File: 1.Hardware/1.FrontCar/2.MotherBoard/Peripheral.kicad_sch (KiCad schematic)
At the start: 11 parts

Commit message: update .gitignore
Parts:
- removed C? (x2): 0.1uF, symbol Device:C_Small
- removed Q?: S8050, Package_TO_SOT_SMD:SOT-23, symbol Device:Q_NPN_BEC
- removed R?: 1K, symbol Device:R_Small
- removed R?: 10K, symbol Device:R_Small
- removed R?: 10R, symbol Device:R_Small
- removed SW?: SW_DIP_x04, symbol Switch:SW_DIP_x04
- removed U?: IPS114, ErBW_s:IPS114, symbol ErBW_s:IPS114
- added BZ?: (no value), symbol Device:Buzzer
- added C?: 100nF, Capacitor_SMD:C_0603_1608Metric, symbol Device:C_Small
- added Q?: (no value), symbol Transistor_BJT:S8050
- added R?: 5K1, symbol Device:R_Small
- IC?: value SN74LVC244APW -> (none); footprint SOP65P640X120-20N -> (none)
- SW?: value SW_5DIR -> (none); footprint ErBW_s:SW_5DIR -> (none)
- U?: value MT9V034 -> (none); footprint Connector_FFC-FPC:Hirose_FH12-18S-0.5SH_1x18-1MP_P0.50mm_Horizontal -> (none)
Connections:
- net GND: now also IC?.1 (1~{OE}), IC?.19 (2~{OE}), SW?.1 (GND), U?.16 (GND), U?.2 (GND), U?.7 (GND), U?.MP (NC), C?.2, Q?.2 (E), R?.2
- net KEY_LEFT: now reaches SW?.2 (L)
- net KEY_LEFT: now also SW?.6 (U)
- net KEY_CENTER: now reaches SW?.3 (C)
- net KEY_RIGHT: now reaches SW?.4 (D)
- net KEY_RIGHT: now also SW?.5 (R)
- net CAM_PLCK: now reaches U?.1 (PCLK)
- net CAM_D2: now reaches U?.10 (D2)
- net CAM_D3: now reaches U?.11 (D3)
- net CAM_D4: now reaches U?.12 (D4)
- net CAM_D5: now reaches U?.13 (D5)
- net CAM_D6: now reaches U?.14 (D6)
- net CAM_D7: now reaches U?.15 (D7)
- net CAM_3V3: now reaches U?.17 (VCC)
- net CAM_3V3: now also U?.18 (VCC)
- net CAM_TXD: now reaches U?.3 (TX)
- net CAM_RXD: now reaches U?.4 (RX)
- net CAM_VSYNC: now reaches U?.6 (VSYNC)
- net CAM_D0: now reaches U?.8 (D0)
- net CAM_D1: now reaches U?.9 (D1)
- net MCU_SERVO: now reaches IC?.11 (2A1)
- net MCU_RDIR: now reaches IC?.12 (1Y4)
- net MCU_RLSB: now reaches IC?.14 (1Y3)
- net MCU_LDIR: now reaches IC?.16 (1Y2)
- net MCU_LLSB: now reaches IC?.18 (1Y1)
- net LLSB: now reaches IC?.2 (1A1)
- net 3V3: now reaches IC?.20 (VCC)
- net 3V3: now also BZ?.1 (-), C?.1
- net LDIR: now reaches IC?.4 (1A2)
- net RLSB: now reaches IC?.6 (1A3)
- net RDIR: now reaches IC?.8 (1A4)
- net SERVO: now reaches IC?.9 (2Y1)
- new net: BZ?.2 (+), Q?.3 (C)
- new net BUZZER: Q?.1 (B), R?.1
- no-connect marks 0 -> 1
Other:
- moved on the sheet: IC?, SW?, U?

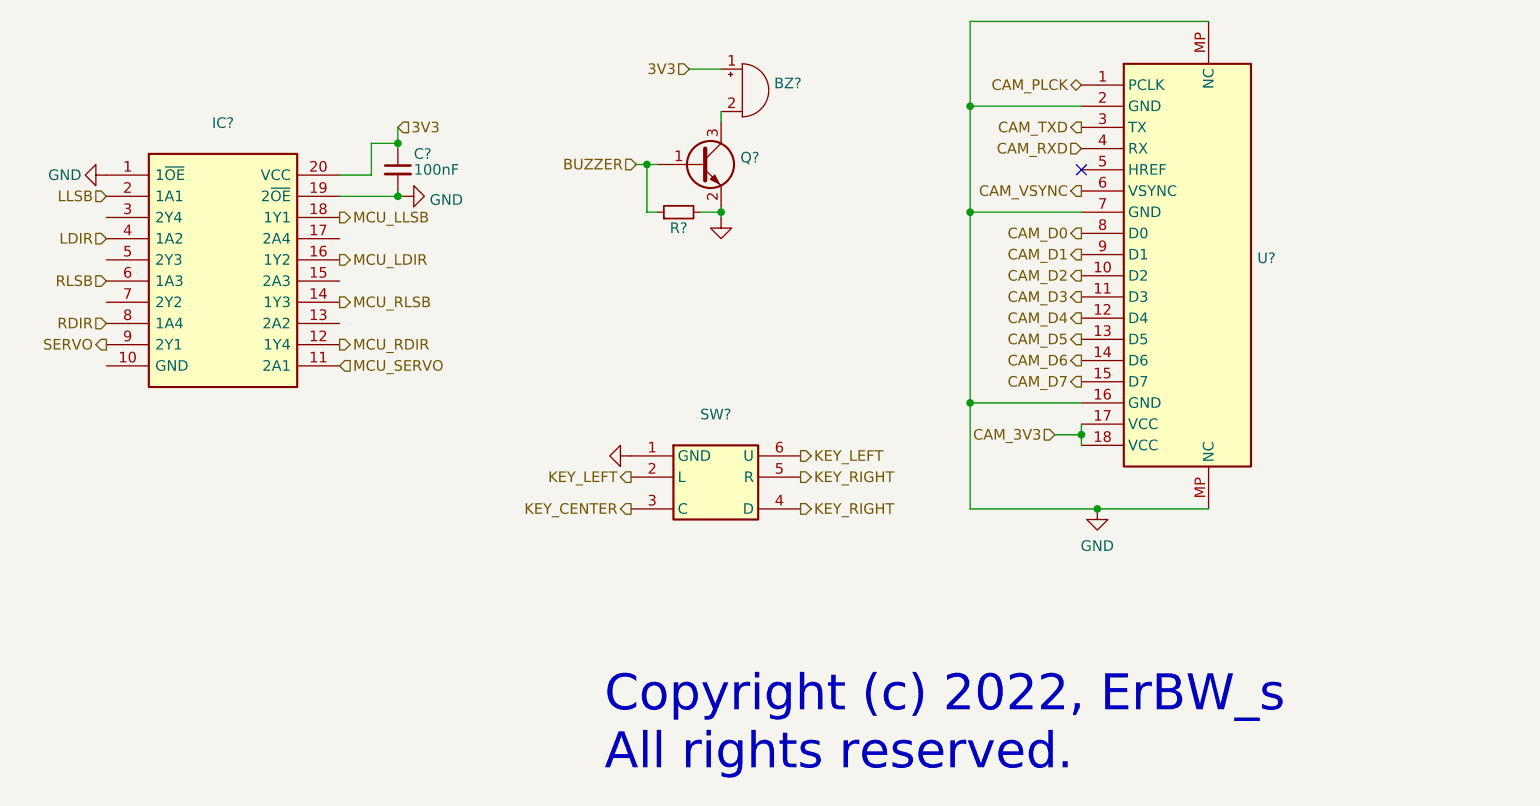
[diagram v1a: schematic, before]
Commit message: 母板原理图完成
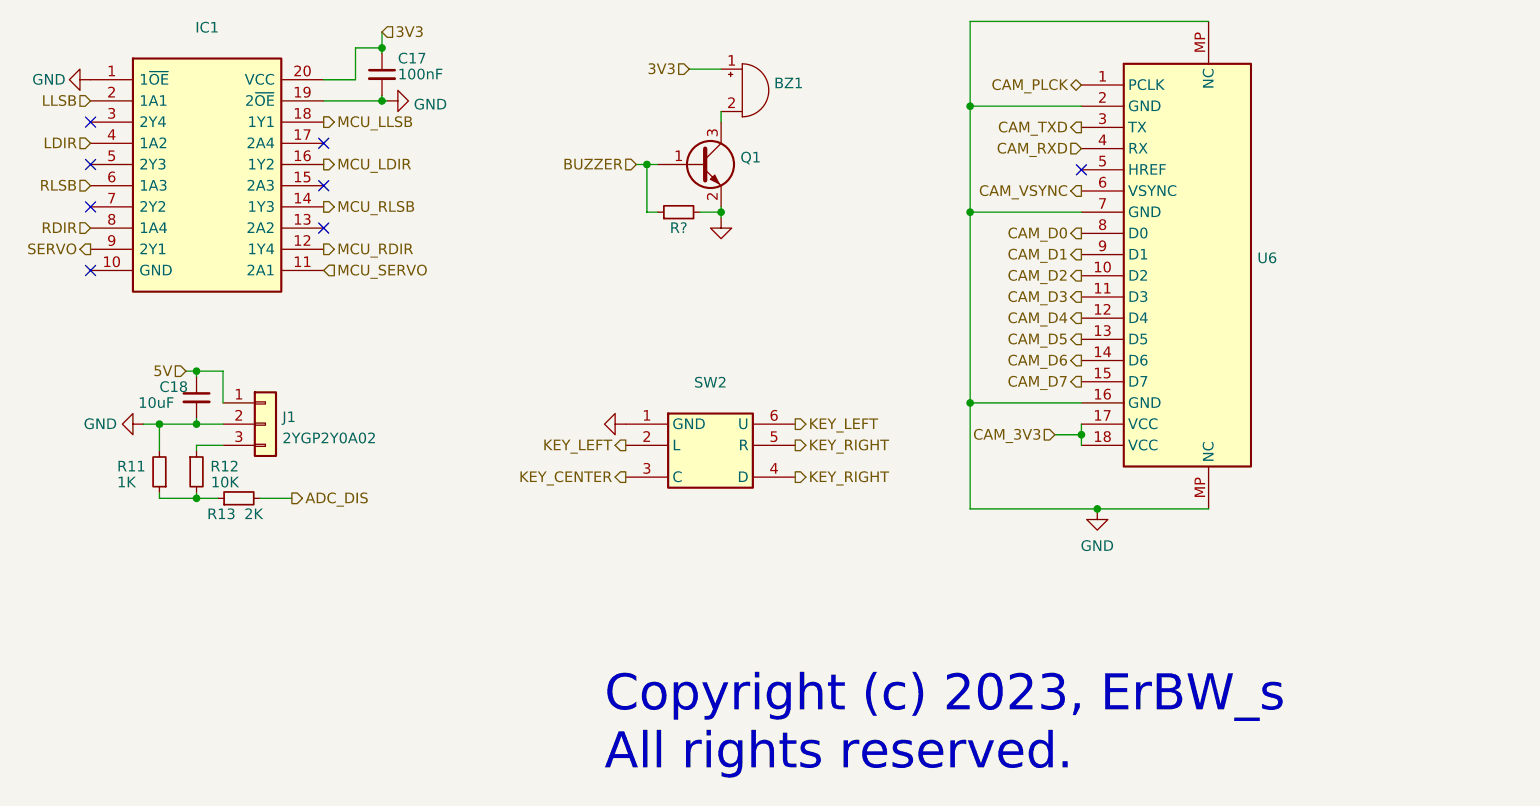
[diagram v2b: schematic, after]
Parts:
- added C18: 10uF, Capacitor_SMD:C_0603_1608Metric, symbol Device:C_Small
- added J1: 2YGP2Y0A02, symbol Connector_Generic:Conn_01x03
- added R11: 1K, Resistor_SMD:R_1206_3216Metric_Pad1.30x1.75mm_HandSolder, symbol Device:R_Small
- added R12: 10K, Resistor_SMD:R_1206_3216Metric_Pad1.30x1.75mm_HandSolder, symbol Device:R_Small
- added R13: 2K, Resistor_SMD:R_1206_3216Metric_Pad1.30x1.75mm_HandSolder, symbol Device:R_Small
- gave numbers to parts that had none: 6
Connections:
- net GND: now also C18.2, J1.2 (Pin_2), R11.2
- new net: R11.1, R12.2, R13.1
- new net: J1.3 (Pin_3), R12.1
- new net 5V: C18.1, J1.1 (Pin_1)
- new net ADC_DIS: R13.2
- no-connect marks 1 -> 8
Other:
- note added: "Copyright (c) 2023, ErBW_s All rights reserved."
- note removed: "Copyright (c) 2022, ErBW_s All rights reserved."
- moved on the sheet: C17, IC1, SW2

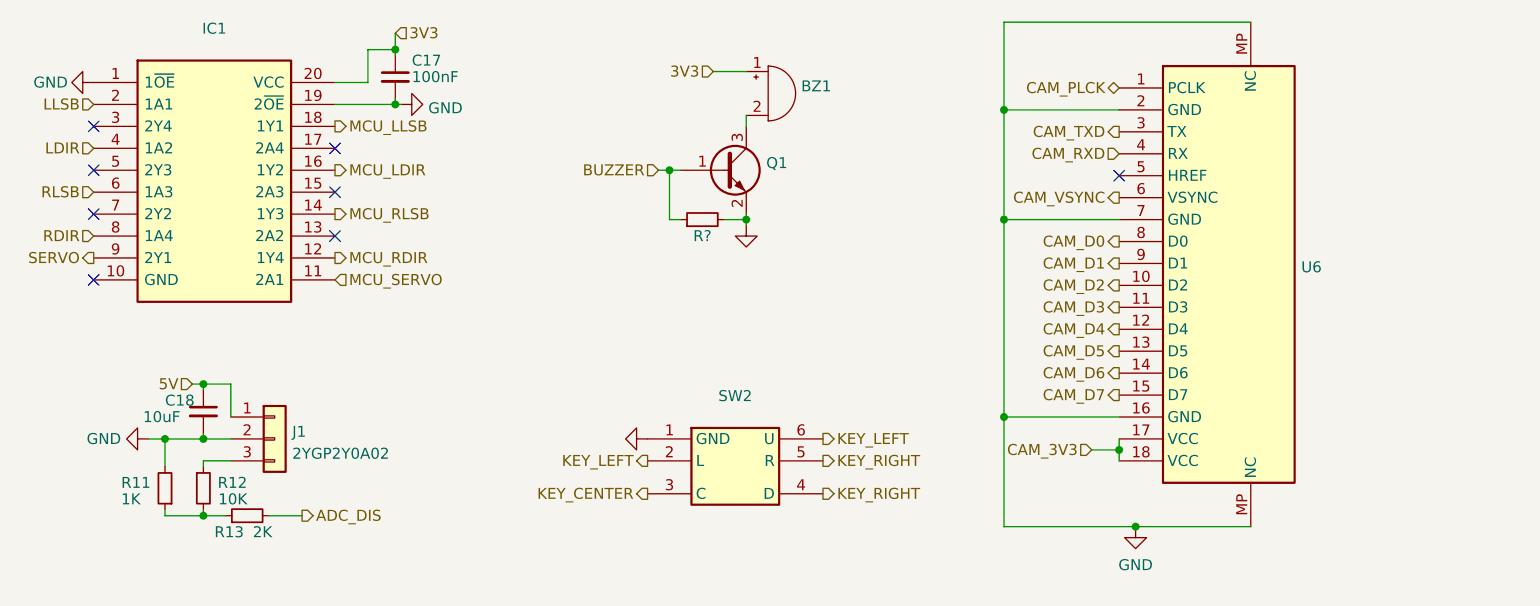
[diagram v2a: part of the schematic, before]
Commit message: 更新母板原理图封装
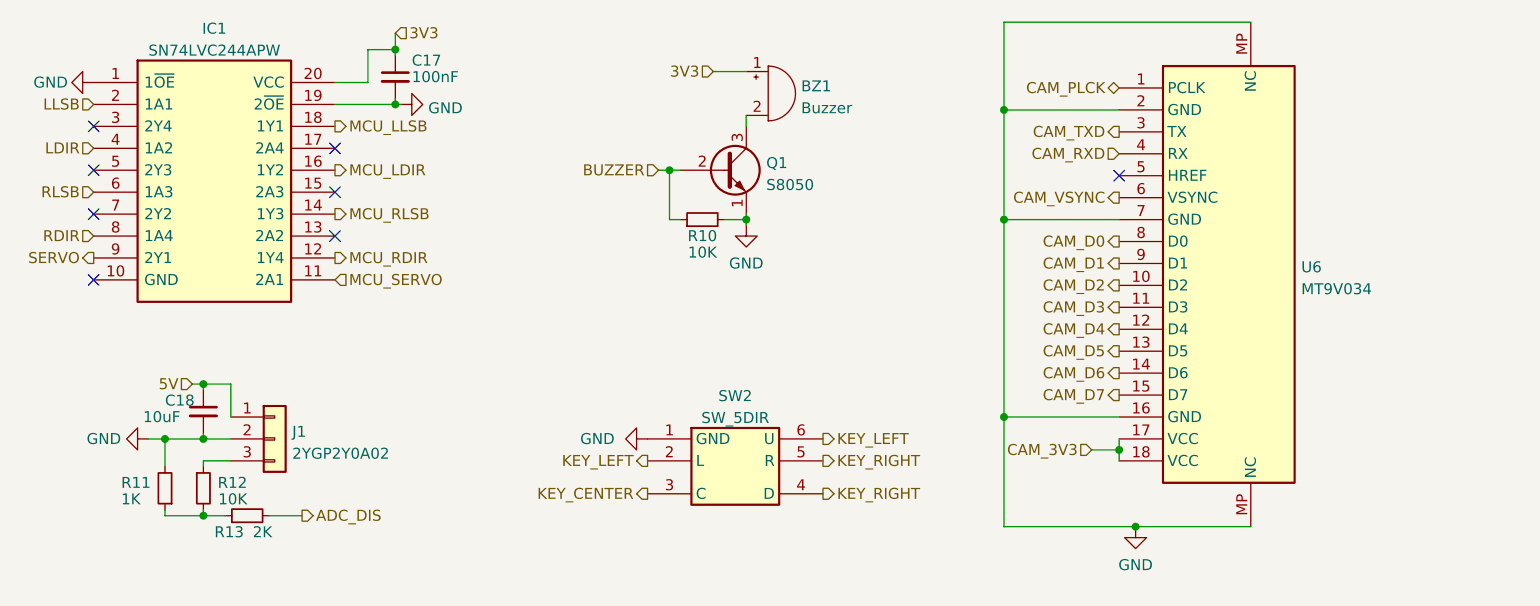
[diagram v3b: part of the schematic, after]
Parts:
- BZ1: value (none) -> Buzzer; footprint (none) -> ErBW_s:Buzzer_9*9P5
- IC1: value (none) -> SN74LVC244APW; footprint (none) -> Package_SO:SOP65P640X120-20N
- J1: footprint (none) -> Connector_PinHeader_2.54mm:PinHeader_1x03_P2.54mm_Vertical
- Q1: value (none) -> S8050; footprint (none) -> Package_TO_SOT_SMD:SOT-23
- R10: renamed from R?; footprint (none) -> Resistor_SMD:R_0603_1608Metric
- R11, R12, R13: footprint Resistor_SMD:R_1206_3216Metric_Pad1.30x1.75mm_HandSolder -> Resistor_SMD:R_0603_1608Metric
- SW2: value (none) -> SW_5DIR; footprint (none) -> ErBW_s:SW_5DIR
- U6: value (none) -> MT9V034; footprint (none) -> Connector_FFC-FPC:Hirose_FH12-18S-0.5SH_1x18-1MP_P0.50mm_Horizontal
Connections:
- net BUZZER: now also Q1.2 (B); no longer Q1.1 (B)
- net GND: now also Q1.1 (E); no longer Q1.2 (E)

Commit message: 母板pcb初步排布
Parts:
- IC1: footprint Package_SO:SOP65P640X120-20N -> ErBW_s:SOP65P640X120-20N
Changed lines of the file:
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@@
       (effects (font (size 1.27 1.27)))
     )
-    (property "Footprint" "Package_SO:SOP65P640X120-20N" (at 60.325 32.385 0)
+    (property "Footprint" "ErBW_s:SOP65P640X120-20N" (at 60.325 32.385 0)
       (effects (font (size 1.27 1.27)) (justify left) hide)
     )
